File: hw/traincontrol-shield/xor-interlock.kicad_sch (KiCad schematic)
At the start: 4 parts, among them U3 74LVC1G86, U4 74LVC2G08

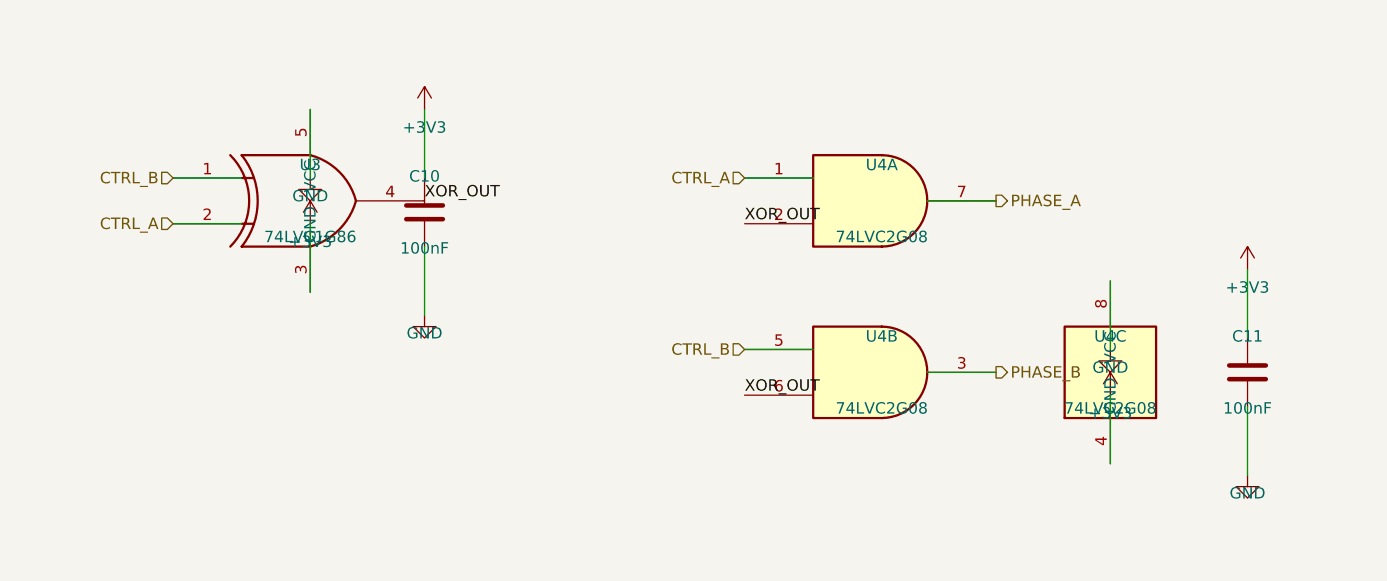
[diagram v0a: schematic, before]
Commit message: Fix hlabel stub direction: stubs now extend away from IC, not into it
Root cause: hlabel() used dx = +STUB for angle=180 and -STUB for angle=0,
which caused every stub wire to run INTO the IC body instead of outward.
This made wires appear to connect at the inner (wrong) end of all pins.

Fix: negate dx so stubs always extend outward from the pin tip:
  angle=180 (left-side input):  dx = -STUB → stub extends LEFT  ✓
  angle=0   (right-side output): dx = +STUB → stub extends RIGHT ✓

Also revert the x-position workarounds that compensated for the wrong
stub direction (zero-crossing AC_IN, opto-triac PHASE/GATE, power-supply
AC_IN/RTN): these are now back at the actual component pin positions.

All 8 sheets validate with kicad-cli.

Co-Authored-By: Claude Sonnet 4.6 <noreply@anthropic.com>
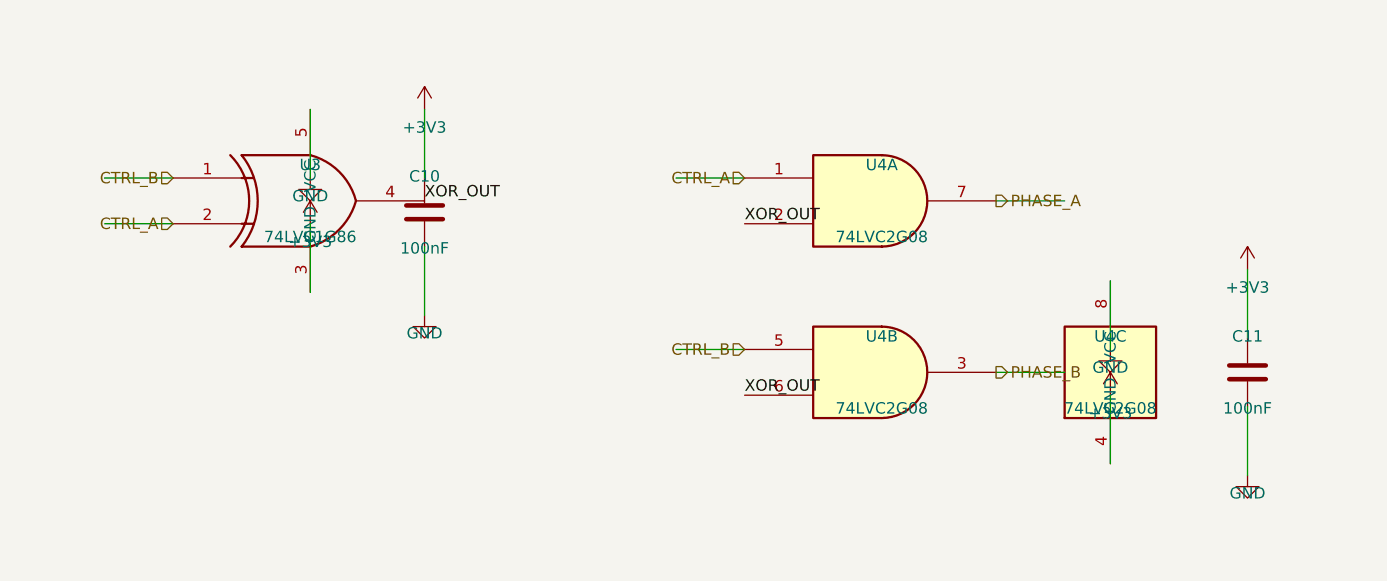
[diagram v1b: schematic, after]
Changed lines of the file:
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@@
 	)
 	(wire
-		(pts (xy 48.26 92.71) (xy 55.879999999999995 92.71))
+		(pts (xy 40.64 92.71) (xy 48.26 92.71))
 		(stroke (width 0) (type solid))
 	)
@@
 	)
 	(wire
-		(pts (xy 48.26 87.63) (xy 55.879999999999995 87.63))
+		(pts (xy 40.64 87.63) (xy 48.26 87.63))
 		(stroke (width 0) (type solid))
 	)
@@
 	)
 	(wire
-		(pts (xy 111.76 87.63) (xy 119.38000000000001 87.63))
+		(pts (xy 104.14 87.63) (xy 111.76 87.63))
 		(stroke (width 0) (type solid))
 	)
@@
 	)
 	(wire
-		(pts (xy 111.76 106.68) (xy 119.38000000000001 106.68))
+		(pts (xy 104.14 106.68) (xy 111.76 106.68))
 		(stroke (width 0) (type solid))
 	)
@@
 	)
 	(wire
-		(pts (xy 132.07999999999998 90.17) (xy 139.7 90.17))
+		(pts (xy 139.7 90.17) (xy 147.32 90.17))
 		(stroke (width 0) (type solid))
 	)
@@
 	)
 	(wire
-		(pts (xy 132.07999999999998 109.22) (xy 139.7 109.22))
+		(pts (xy 139.7 109.22) (xy 147.32 109.22))
 		(stroke (width 0) (type solid))
 	)

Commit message: Fix hlabel placement: label sits at stub outer end (lx), not pin tip (x)
The hierarchical label connection point must be at lx (the outer end of
the stub wire), not at x (the IC pin tip). With the label at x, it was
overlapping the pin itself instead of sitting at the end of the routing
stub where it belongs.

  angle=180 (left-side): lx = x - STUB  → label to the left of pin ✓
  angle=0   (right-side): lx = x + STUB  → label to the right of pin ✓

Wire still runs x↔lx, connecting the IC pin to the label connection.
Updated gen_all_sheets.py and gen_power_supply.py.

Co-Authored-By: Claude Sonnet 4.6 <noreply@anthropic.com>
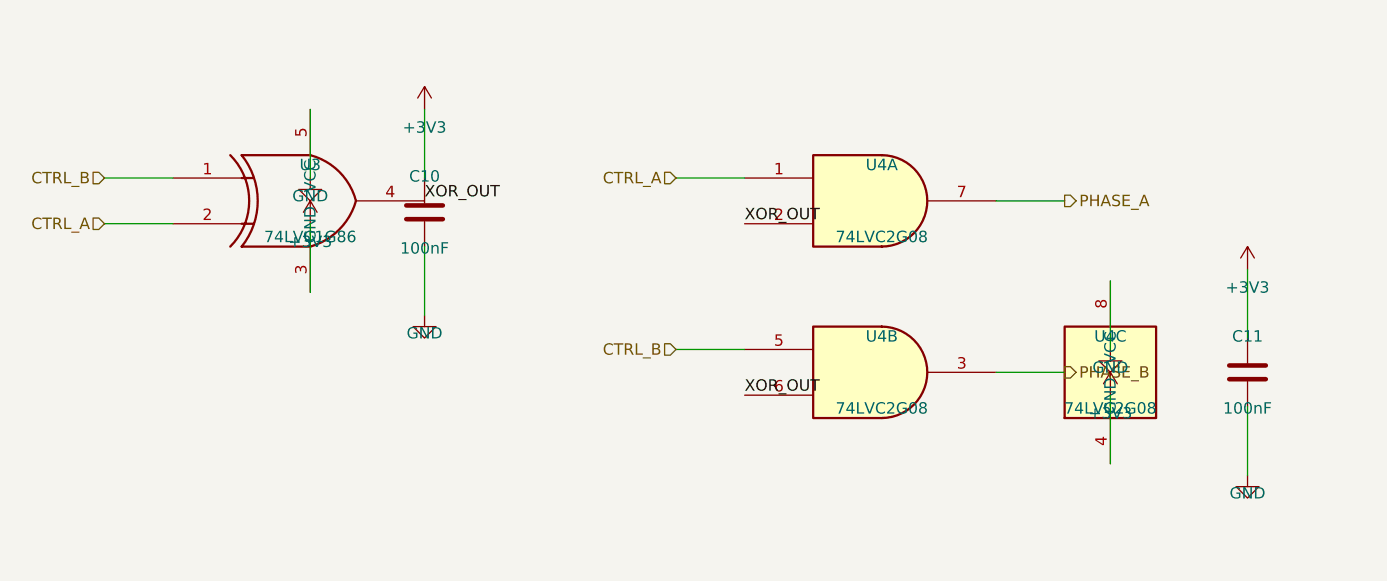
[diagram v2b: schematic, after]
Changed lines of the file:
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@@
 	(hierarchical_label "CTRL_A"
 		(shape input)
-		(at 48.26 92.71 180)
+		(at 40.64 92.71 180)
 		(fields_autoplaced yes)
 		(effects (font (size 1.27 1.27)) (justify right bottom))
 		(property "Intersheetrefs" "${INTERSHEET_REFS}"
-			(at 48.26 92.71 0)
+			(at 40.64 92.71 0)
 			(effects (font (size 1.27 1.27)) (hide yes))
 		)
@@
 	(hierarchical_label "CTRL_B"
 		(shape input)
-		(at 48.26 87.63 180)
+		(at 40.64 87.63 180)
 		(fields_autoplaced yes)
 		(effects (font (size 1.27 1.27)) (justify right bottom))
 		(property "Intersheetrefs" "${INTERSHEET_REFS}"
-			(at 48.26 87.63 0)
+			(at 40.64 87.63 0)
 			(effects (font (size 1.27 1.27)) (hide yes))
 		)
@@
 	(hierarchical_label "CTRL_A"
 		(shape input)
-		(at 111.76 87.63 180)
+		(at 104.14 87.63 180)
 		(fields_autoplaced yes)
 		(effects (font (size 1.27 1.27)) (justify right bottom))
 		(property "Intersheetrefs" "${INTERSHEET_REFS}"
-			(at 111.76 87.63 0)
+			(at 104.14 87.63 0)
 			(effects (font (size 1.27 1.27)) (hide yes))
 		)
@@
 	(hierarchical_label "CTRL_B"
 		(shape input)
-		(at 111.76 106.68 180)
+		(at 104.14 106.68 180)
 		(fields_autoplaced yes)
 		(effects (font (size 1.27 1.27)) (justify right bottom))
 		(property "Intersheetrefs" "${INTERSHEET_REFS}"
-			(at 111.76 106.68 0)
+			(at 104.14 106.68 0)
 			(effects (font (size 1.27 1.27)) (hide yes))
 		)
@@
 	(hierarchical_label "PHASE_A"
 		(shape output)
-		(at 139.7 90.17 0)
+		(at 147.32 90.17 0)
 		(fields_autoplaced yes)
 		(effects (font (size 1.27 1.27)) (justify left bottom))
 		(property "Intersheetrefs" "${INTERSHEET_REFS}"
-			(at 139.7 90.17 0)
+			(at 147.32 90.17 0)
 			(effects (font (size 1.27 1.27)) (hide yes))
 		)
@@
 	(hierarchical_label "PHASE_B"
 		(shape output)
-		(at 139.7 109.22 0)
+		(at 147.32 109.22 0)
 		(fields_autoplaced yes)
 		(effects (font (size 1.27 1.27)) (justify left bottom))
 		(property "Intersheetrefs" "${INTERSHEET_REFS}"
-			(at 139.7 109.22 0)
+			(at 147.32 109.22 0)
 			(effects (font (size 1.27 1.27)) (hide yes))
 		)

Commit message: Add wire stub to net_label, matching hlabel placement convention
net_label() now generates a short wire stub (length STUB) between the
component pin tip (x) and the label connection point (lx), placing the
label at the outer end of the stub — identical to how hlabel works:

  angle=180 (left-side):  lx = x - STUB, label left of pin  ✓
  angle=0   (right-side): lx = x + STUB, label right of pin ✓

Also fix XOR_OUT net labels at U4A/B left-side input pins (angle=0→180)
so their stubs extend leftward away from the IC body.

Updated gen_all_sheets.py and gen_power_supply.py.

Co-Authored-By: Claude Sonnet 4.6 <noreply@anthropic.com>
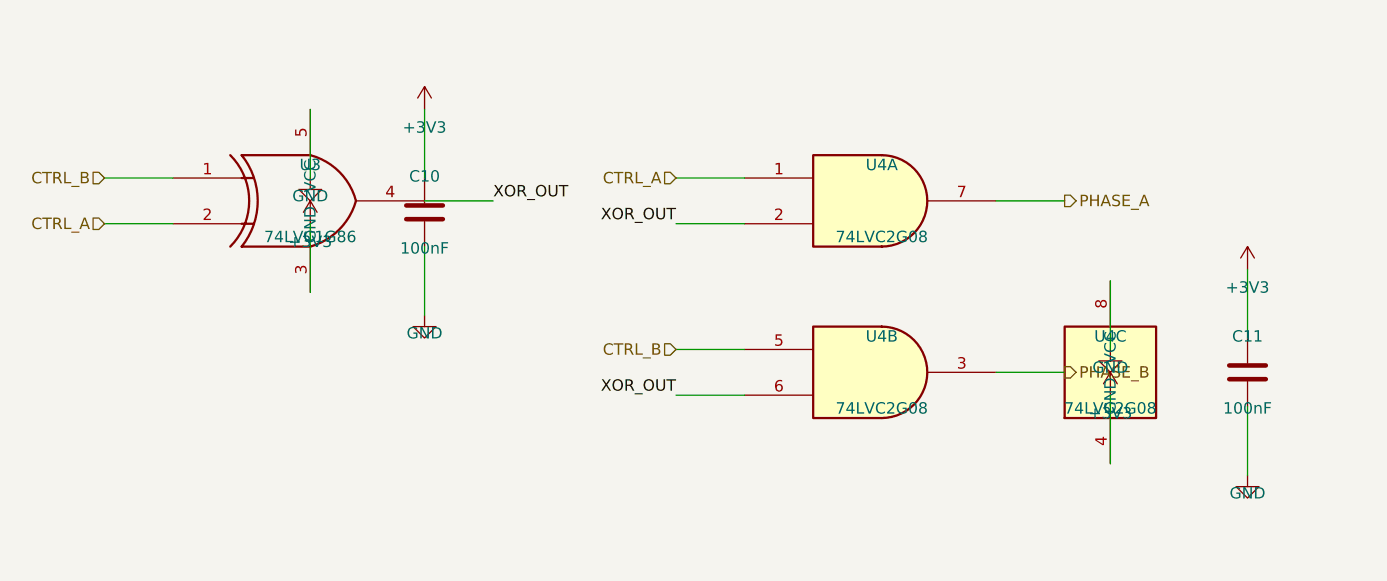
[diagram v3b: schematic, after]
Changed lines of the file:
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@@
 		)
 	)
-	(label "XOR_OUT"
-		(at 76.2 90.17 0)
-		(fields_autoplaced yes)
-		(effects (font (size 1.27 1.27)) (justify left bottom))
+	(wire
+		(pts (xy 76.2 90.17) (xy 83.82000000000001 90.17))
+		(stroke (width 0) (type solid))
 	)
 	(label "XOR_OUT"
-		(at 111.76 92.71 0)
-		(fields_autoplaced yes)
-		(effects (font (size 1.27 1.27)) (justify left bottom))
-	)
-	(label "XOR_OUT"
-		(at 111.76 111.76 0)
+		(at 83.82000000000001 90.17 0)
 		(fields_autoplaced yes)
 		(effects (font (size 1.27 1.27)) (justify left bottom))
 	)
 	(wire
+		(pts (xy 104.14 92.71) (xy 111.76 92.71))
+		(stroke (width 0) (type solid))
+	)
+	(label "XOR_OUT"
+		(at 104.14 92.71 180)
+		(fields_autoplaced yes)
+		(effects (font (size 1.27 1.27)) (justify right bottom))
+	)
+	(wire
+		(pts (xy 104.14 111.76) (xy 111.76 111.76))
+		(stroke (width 0) (type solid))
+	)
+	(label "XOR_OUT"
+		(at 104.14 111.76 180)
+		(fields_autoplaced yes)
+		(effects (font (size 1.27 1.27)) (justify right bottom))
+	)
+	(wire

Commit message: Increase component spacing to eliminate pin-wire overlaps
- zero-crossing: move R1 left 7.62mm, add bridge wire to U2 pin2
- xor-interlock: move C10 right of U3 output (76→91mm), move C11 right (168→178mm)
- opto-triac: add 7.62mm COMP_GAP between MOC3021 and LED/gate resistors
- triacs-snubbers: move snubber column right (99→109mm), add 7.62mm gap between R and C
- mcu: widen C4/C5/C6 decap spacing from 7.62mm to 10.16mm
- power-supply: move R13 down 7.62mm, add bridge wire to R12

Co-Authored-By: Claude Sonnet 4.6 <noreply@anthropic.com>
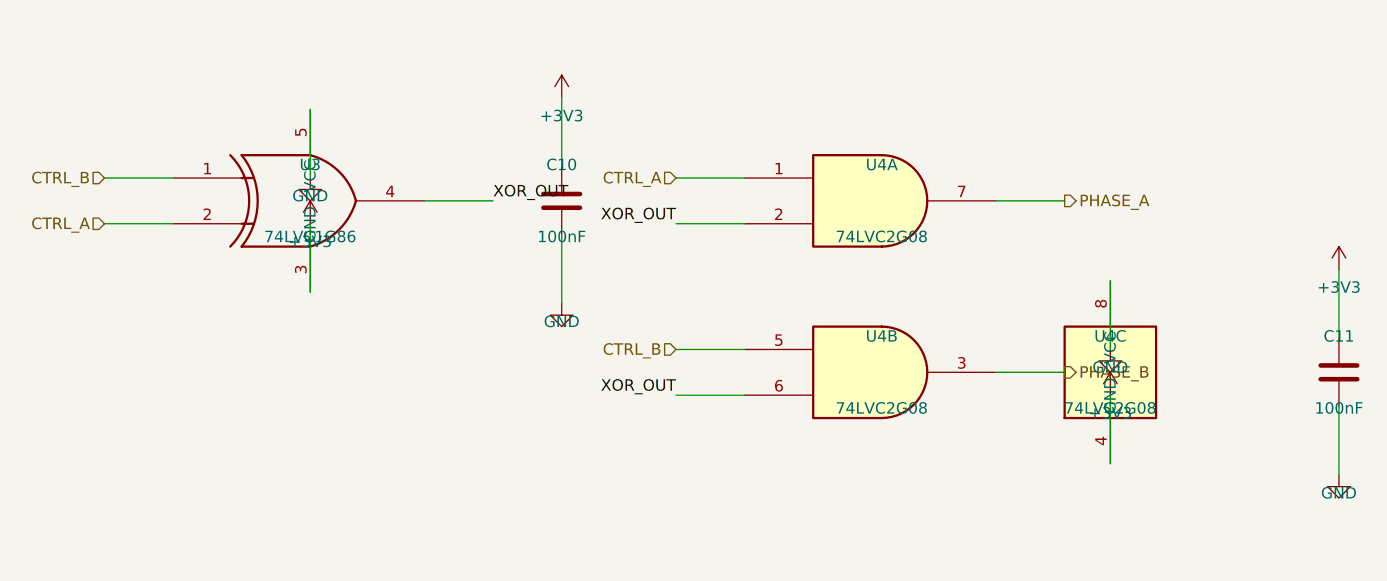
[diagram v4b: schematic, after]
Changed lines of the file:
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@@
 	(symbol
 		(lib_id "Device:C")
-		(at 76.2 91.44 180)
+		(at 91.44 90.17 180)
 		(unit 1)
 		(exclude_from_sim no)
@@
 		(dnp no)
 		(property "Reference" "C10"
-			(at 76.2 87.44 0)
+			(at 91.44 86.17 0)
 			(effects (font (size 1.27 1.27)))
 		)
 		(property "Value" "100nF"
-			(at 76.2 95.44 0)
+			(at 91.44 94.17 0)
 			(effects (font (size 1.27 1.27)))
 		)
 		(property "Footprint" "Capacitor_SMD:C_0603_1608Metric"
-			(at 76.2 91.44 0)
-			(effects (font (size 1.27 1.27)) (hide yes))
-		)
-		(property "Datasheet" "~"
-			(at 76.2 91.44 0)
+			(at 91.44 90.17 0)
+			(effects (font (size 1.27 1.27)) (hide yes))
+		)
+		(property "Datasheet" "~"
+			(at 91.44 90.17 0)
 			(effects (font (size 1.27 1.27)) (hide yes))
 		)
@@
 	)
 	(wire
-		(pts (xy 76.2 87.63) (xy 76.2 80.00999999999999))
+		(pts (xy 91.44 86.36) (xy 91.44 78.74))
 		(stroke (width 0) (type solid))
 	)
 	(symbol
 		(lib_id "power:+3V3")
-		(at 76.2 80.00999999999999 0)
+		(at 91.44 78.74 0)
 		(unit 1)
 		(exclude_from_sim no)
@@
 		(dnp no)
 		(property "Reference" "#PWR0403"
-			(at 76.2 78.00999999999999 0)
+			(at 91.44 76.74 0)
 			(effects (font (size 1.27 1.27)) (hide yes))
 		)
 		(property "Value" "+3V3"
-			(at 76.2 82.00999999999999 0)
-			(effects (font (size 1.27 1.27)))
-		)
-		(property "Footprint" ""
-			(at 76.2 80.00999999999999 0)
-			(effects (font (size 1.27 1.27)) (hide yes))
-		)
-		(property "Datasheet" ""
-			(at 76.2 80.00999999999999 0)
+			(at 91.44 80.74 0)
+			(effects (font (size 1.27 1.27)))
+		)
+		(property "Footprint" ""
+			(at 91.44 78.74 0)
+			(effects (font (size 1.27 1.27)) (hide yes))
+		)
+		(property "Datasheet" ""
+			(at 91.44 78.74 0)
 			(effects (font (size 1.27 1.27)) (hide yes))
 		)
@@
 	)
 	(wire
-		(pts (xy 76.2 95.25) (xy 76.2 102.87))
+		(pts (xy 91.44 93.98) (xy 91.44 101.60000000000001))
 		(stroke (width 0) (type solid))
 	)
 	(symbol
 		(lib_id "power:GND")
-		(at 76.2 102.87 0)
+		(at 91.44 101.60000000000001 0)
 		(unit 1)
 		(exclude_from_sim no)
@@
 		(dnp no)
 		(property "Reference" "#PWR0404"
-			(at 76.2 100.87 0)
+			(at 91.44 99.60000000000001 0)
 			(effects (font (size 1.27 1.27)) (hide yes))
 		)
 		(property "Value" "GND"
-			(at 76.2 104.87 0)
-			(effects (font (size 1.27 1.27)))
-		)
-		(property "Footprint" ""
-			(at 76.2 102.87 0)
-			(effects (font (size 1.27 1.27)) (hide yes))
-		)
-		(property "Datasheet" ""
-			(at 76.2 102.87 0)
+			(at 91.44 103.60000000000001 0)
+			(effects (font (size 1.27 1.27)))
+		)
+		(property "Footprint" ""
+			(at 91.44 101.60000000000001 0)
+			(effects (font (size 1.27 1.27)) (hide yes))
+		)
+		(property "Datasheet" ""
+			(at 91.44 101.60000000000001 0)
 			(effects (font (size 1.27 1.27)) (hide yes))
 		)
@@
 	(symbol
 		(lib_id "Device:C")
-		(at 167.64 109.22 180)
+		(at 177.8 109.22 180)
 		(unit 1)
 		(exclude_from_sim no)
@@
 		(dnp no)
 		(property "Reference" "C11"
-			(at 167.64 105.22 0)
+			(at 177.8 105.22 0)
 			(effects (font (size 1.27 1.27)))
 		)
 		(property "Value" "100nF"
-			(at 167.64 113.22 0)
+			(at 177.8 113.22 0)
 			(effects (font (size 1.27 1.27)))
 		)
 		(property "Footprint" "Capacitor_SMD:C_0603_1608Metric"
-			(at 167.64 109.22 0)
-			(effects (font (size 1.27 1.27)) (hide yes))
-		)
-		(property "Datasheet" "~"
-			(at 167.64 109.22 0)
+			(at 177.8 109.22 0)
+			(effects (font (size 1.27 1.27)) (hide yes))
+		)
+		(property "Datasheet" "~"
+			(at 177.8 109.22 0)
 			(effects (font (size 1.27 1.27)) (hide yes))
 		)
@@
 	)
 	(wire
-		(pts (xy 167.64 105.41) (xy 167.64 97.78999999999999))
+		(pts (xy 177.8 105.41) (xy 177.8 97.78999999999999))
 		(stroke (width 0) (type solid))
 	)
 	(symbol
 		(lib_id "power:+3V3")
-		(at 167.64 97.78999999999999 0)
+		(at 177.8 97.78999999999999 0)
 		(unit 1)
 		(exclude_from_sim no)
@@
 		(dnp no)
 		(property "Reference" "#PWR0407"
-			(at 167.64 95.78999999999999 0)
+			(at 177.8 95.78999999999999 0)
 			(effects (font (size 1.27 1.27)) (hide yes))
 		)
 		(property "Value" "+3V3"
-			(at 167.64 99.78999999999999 0)
-			(effects (font (size 1.27 1.27)))
-		)
-		(property "Footprint" ""
-			(at 167.64 97.78999999999999 0)
-			(effects (font (size 1.27 1.27)) (hide yes))
-		)
-		(property "Datasheet" ""
-			(at 167.64 97.78999999999999 0)
+			(at 177.8 99.78999999999999 0)
+			(effects (font (size 1.27 1.27)))
+		)
+		(property "Footprint" ""
+			(at 177.8 97.78999999999999 0)
+			(effects (font (size 1.27 1.27)) (hide yes))
+		)
+		(property "Datasheet" ""
+			(at 177.8 97.78999999999999 0)
 			(effects (font (size 1.27 1.27)) (hide yes))
 		)
@@
 	)
 	(wire
-		(pts (xy 167.64 113.03) (xy 167.64 120.65))
+		(pts (xy 177.8 113.03) (xy 177.8 120.65))
 		(stroke (width 0) (type solid))
 	)
 	(symbol
 		(lib_id "power:GND")
-		(at 167.64 120.65 0)
+		(at 177.8 120.65 0)
 		(unit 1)
 		(exclude_from_sim no)
@@
 		(dnp no)
 		(property "Reference" "#PWR0408"
-			(at 167.64 118.65 0)
+			(at 177.8 118.65 0)
 			(effects (font (size 1.27 1.27)) (hide yes))
 		)
 		(property "Value" "GND"
-			(at 167.64 122.65 0)
-			(effects (font (size 1.27 1.27)))
-		)
-		(property "Footprint" ""
-			(at 167.64 120.65 0)
-			(effects (font (size 1.27 1.27)) (hide yes))
-		)
-		(property "Datasheet" ""
-			(at 167.64 120.65 0)
-			(effects (font (size 1.27 1.27)) (hide yes))
-		)
+			(at 177.8 122.65 0)
+			(effects (font (size 1.27 1.27)))
+		)
+		(property "Footprint" ""
+			(at 177.8 120.65 0)
+			(effects (font (size 1.27 1.27)) (hide yes))
+		)
+		(property "Datasheet" ""
+			(at 177.8 120.65 0)
+			(effects (font (size 1.27 1.27)) (hide yes))
+		)
